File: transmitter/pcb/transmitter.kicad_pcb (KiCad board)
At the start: 2 copper layers, 70.5 x 67 mm, 14 parts, among them U1 AMS1117-3.3, U2 MOUDLE-SEEEDUINO-XIAO-ESP32C3

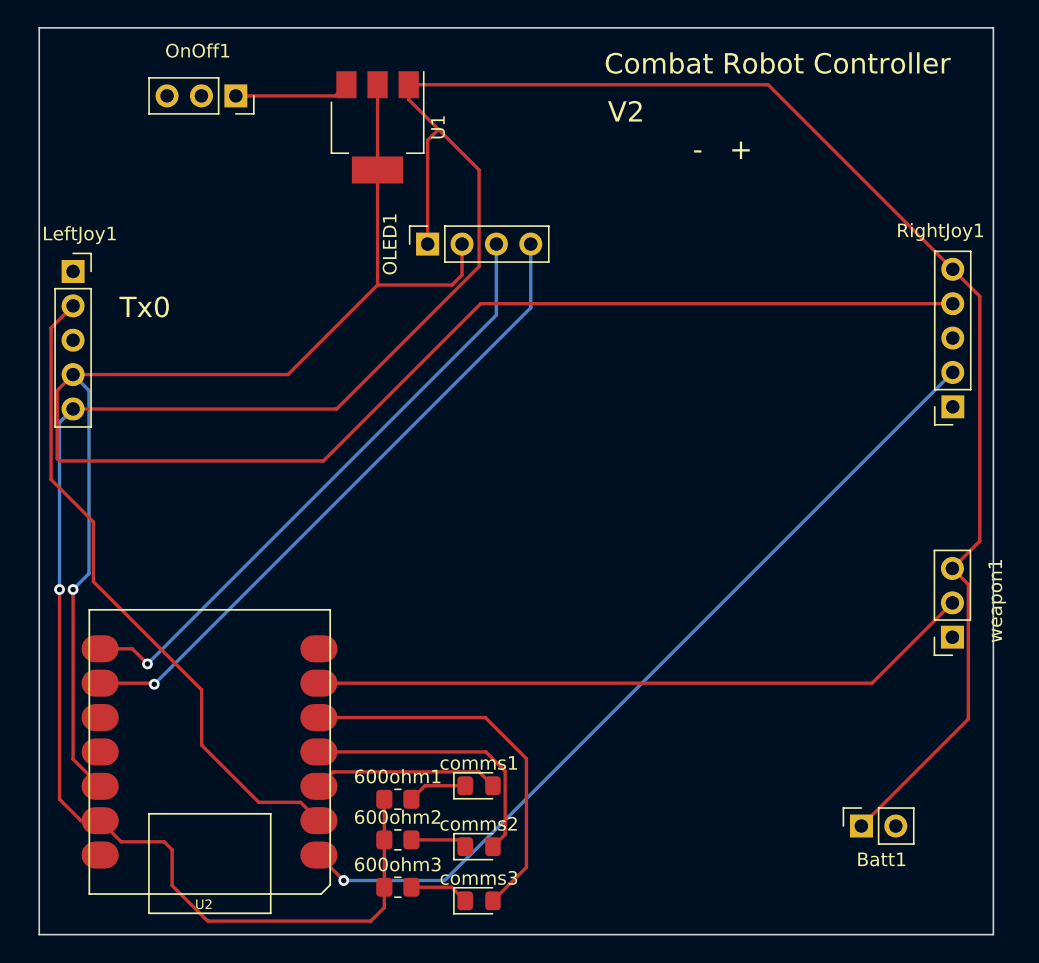
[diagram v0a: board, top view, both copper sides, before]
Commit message: added 9v battery holder footprint and symbol
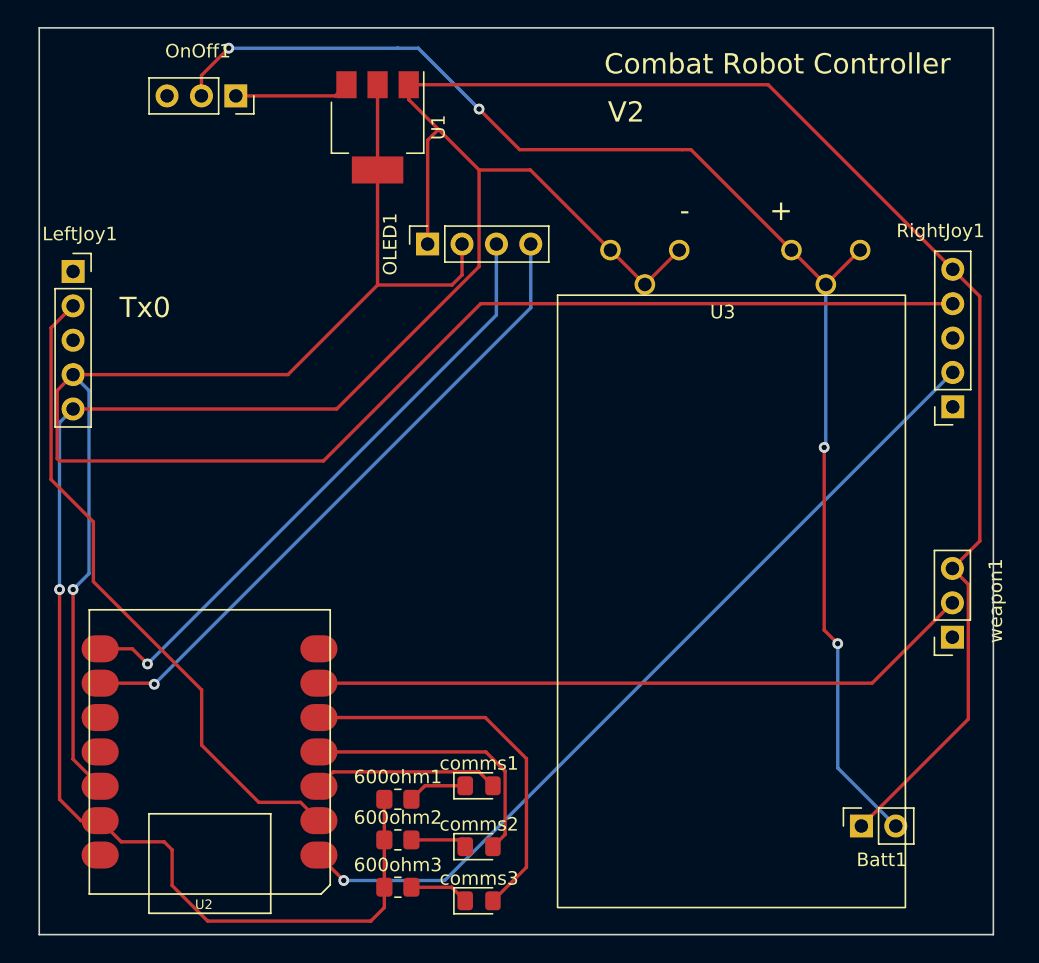
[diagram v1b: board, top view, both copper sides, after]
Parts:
- added U3: 9Vbattery, 9v_battery:9v_battery, F.Cu at (221.0, 61.5)
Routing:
- net +9V: track 8.52 -> 110.4 mm, vias 0 -> 4
- net GND: track 218.1 -> 237.5 mm
